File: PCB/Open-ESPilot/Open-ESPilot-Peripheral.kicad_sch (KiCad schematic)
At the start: 47 parts, among them J10 GND, J11 RC in, J12 LED out, J13 Micro_SD_Card, J14 Micro SD Card, J4 UART0, J5 UART1, J6 UART2, J7 I2C, J8 PWM output, J9 Vx, M2 GY91, Q1 NPN, Q2 NPN

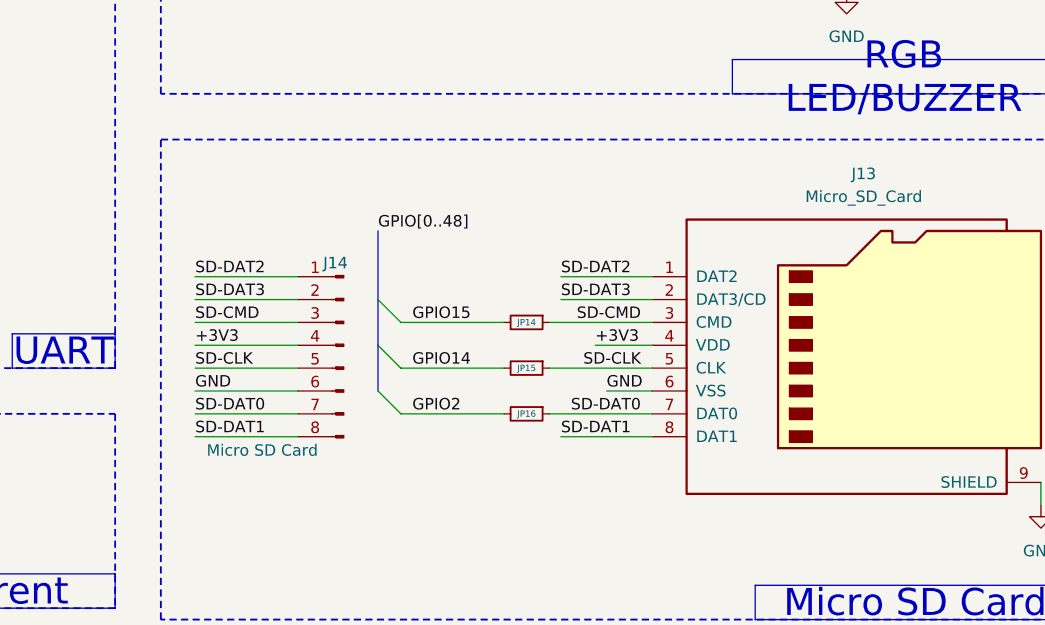
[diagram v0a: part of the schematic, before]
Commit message: Assigned footprints and components for the easy ones (R,C,JP,J)
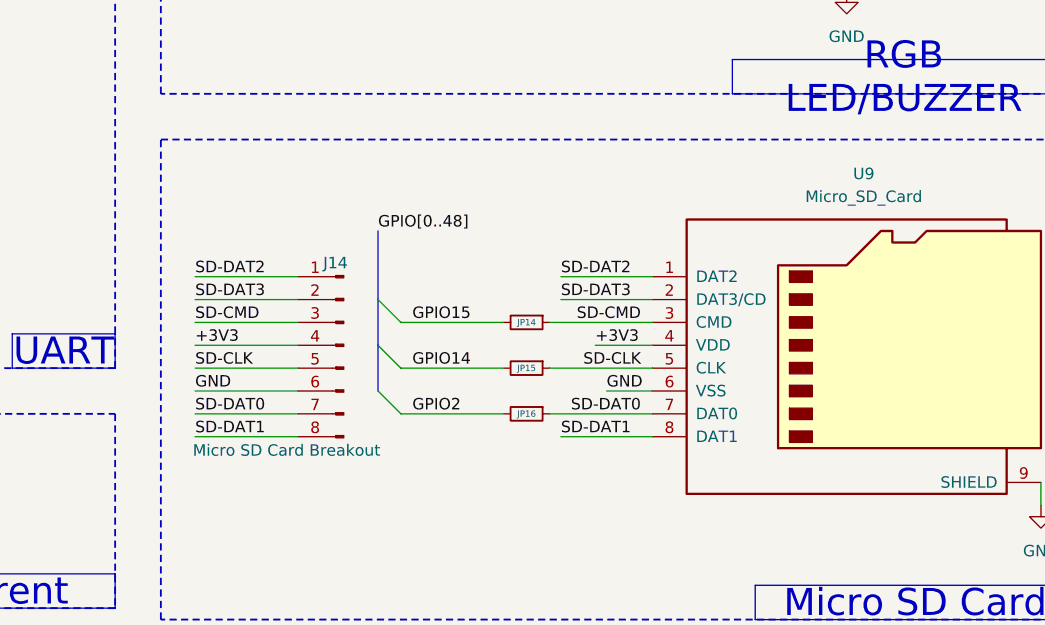
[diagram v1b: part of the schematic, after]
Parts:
- BZ1: footprint Buzzer_Beeper:MagneticBuzzer_StarMicronics_QMB-108 -> (none)
- C8: footprint (none) -> Capacitor_SMD:C_0805_2012Metric_Pad1.18x1.45mm_HandSolder
- J10, J8, J9: footprint (none) -> Connector_PinHeader_2.54mm:PinHeader_1x08_P2.54mm_Vertical
- J11, J12, J4: footprint (none) -> Connector_PinHeader_2.54mm:PinHeader_1x03_P2.54mm_Vertical
- J14: value Micro SD Card -> Micro SD Card Breakout; footprint (none) -> Connector_PinHeader_2.54mm:PinHeader_1x08_P2.54mm_Vertical
- J5, J7: footprint (none) -> Connector_PinHeader_2.54mm:PinHeader_1x04_P2.54mm_Vertical
- J6: footprint (none) -> Connector_PinHeader_2.54mm:PinHeader_1x06_P2.54mm_Vertical
- JP1: footprint (none) -> Jumper:SolderJumper-2_P1.3mm_Bridged2Bar_RoundedPad1.0x1.5mm
- JP2: footprint (none) -> Jumper:SolderJumper-3_P1.3mm_Bridged2Bar12_RoundedPad1.0x1.5mm_NumberLabels
- R10, R11, R5, R6, R7: footprint (none) -> Resistor_SMD:R_0805_2012Metric_Pad1.20x1.40mm_HandSolder
- renumbered J13 to U9
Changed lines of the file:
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@@
 		(dnp no)
 		(fields_autoplaced yes)
-		(property "Reference" "J13"
+		(property "Reference" "U9"
 			(at 255.905 110.49 0)
 			(effects
@@
 			(project ""
 				(path "/2992e60d-a645-4cd7-90ae-fe72311b6bee/e6a81ea1-6816-412d-a6dc-b491c7035238"
-					(reference "J13")
+					(reference "U9")
 					(unit 1)
 				)
@@
 			)
 		)
-		(property "Footprint" ""
+		(property "Footprint" "Connector_PinHeader_2.54mm:PinHeader_1x06_P2.54mm_Vertical"
 			(at 147.32 118.11 0)
 			(effects
@@
 			)
 		)
-		(property "Footprint" ""
+		(property "Footprint" "Connector_PinHeader_2.54mm:PinHeader_1x03_P2.54mm_Vertical"
 			(at 147.32 87.63 0)
 			(effects
@@
 			)
 		)
-		(property "Footprint" "Buzzer_Beeper:MagneticBuzzer_StarMicronics_QMB-108"
+		(property "Footprint" ""
 			(at 258.445 69.85 90)
 			(effects
@@
 			)
 		)
-		(property "Footprint" ""
+		(property "Footprint" "Connector_PinHeader_2.54mm:PinHeader_1x08_P2.54mm_Vertical"
 			(at 91.44 101.6 0)
 			(effects
@@
 			)
 		)
-		(property "Footprint" ""
+		(property "Footprint" "Connector_PinHeader_2.54mm:PinHeader_1x03_P2.54mm_Vertical"
 			(at 83.82 176.53 0)
 			(effects
@@
 			)
 		)
-		(property "Footprint" ""
+		(property "Footprint" "Resistor_SMD:R_0805_2012Metric_Pad1.20x1.40mm_HandSolder"
 			(at 53.34 175.768 90)
 			(effects
@@
 			)
 		)
-		(property "Footprint" ""
+		(property "Footprint" "Resistor_SMD:R_0805_2012Metric_Pad1.20x1.40mm_HandSolder"
 			(at 41.148 160.02 90)
 			(effects
@@
 			)
 		)
-		(property "Footprint" ""
+		(property "Footprint" "Connector_PinHeader_2.54mm:PinHeader_1x03_P2.54mm_Vertical"
 			(at 264.16 39.37 0)
 			(effects
@@
 			)
 		)
-		(property "Footprint" ""
+		(property "Footprint" "Resistor_SMD:R_0805_2012Metric_Pad1.20x1.40mm_HandSolder"
 			(at 103.632 43.18 90)
 			(effects
@@
 			)
 		)
-		(property "Footprint" ""
+		(property "Footprint" "Connector_PinHeader_2.54mm:PinHeader_1x04_P2.54mm_Vertical"
 			(at 147.32 100.33 0)
 			(effects
@@
 			)
 		)
-		(property "Footprint" ""
+		(property "Footprint" "Capacitor_SMD:C_0805_2012Metric_Pad1.18x1.45mm_HandSolder"
 			(at 183.8452 40.64 0)
 			(effects
@@
 			)
 		)
-		(property "Footprint" ""
+		(property "Footprint" "Resistor_SMD:R_0805_2012Metric_Pad1.20x1.40mm_HandSolder"
 			(at 115.062 43.18 90)
 			(effects
@@
 			)
 		)
-		(property "Footprint" ""
+		(property "Footprint" "Jumper:SolderJumper-2_P1.3mm_Bridged2Bar_RoundedPad1.0x1.5mm"
 			(at 69.85 87.63 0)
 			(effects
@@
 			)
 		)
-		(property "Value" "Micro SD Card"
-			(at 182.88 141.224 0)
+		(property "Value" "Micro SD Card Breakout"
+			(at 191.77 141.224 0)
 			(effects
 				(font
 					(size 1.27 1.27)
 				)
-				(justify right)
 			)
 		)
-		(property "Footprint" ""
+		(property "Footprint" "Connector_PinHeader_2.54mm:PinHeader_1x08_P2.54mm_Vertical"
 			(at 198.12 129.54 0)
 			(effects
@@
 			)
 		)
-		(property "Footprint" ""
+		(property "Footprint" "Connector_PinHeader_2.54mm:PinHeader_1x08_P2.54mm_Vertical"
 			(at 77.47 101.6 0)
 			(effects
@@
 			)
 		)
-		(property "Footprint" ""
+		(property "Footprint" "Connector_PinHeader_2.54mm:PinHeader_1x04_P2.54mm_Vertical"
 			(at 162.56 40.64 0)
 			(effects
@@
 			)
 		)
-		(property "Footprint" ""
+		(property "Footprint" "Connector_PinHeader_2.54mm:PinHeader_1x08_P2.54mm_Vertical"
 			(at 62.23 101.6 0)
 			(effects
@@
 			)
 		)
-		(property "Footprint" ""
+		(property "Footprint" "Jumper:SolderJumper-3_P1.3mm_Bridged2Bar12_RoundedPad1.0x1.5mm_NumberLabels"
 			(at 50.8 137.16 0)
 			(effects
@@
 			)
 		)
-		(property "Footprint" ""
+		(property "Footprint" "Resistor_SMD:R_0805_2012Metric_Pad1.20x1.40mm_HandSolder"
 			(at 238.76 84.328 90)
 			(effects

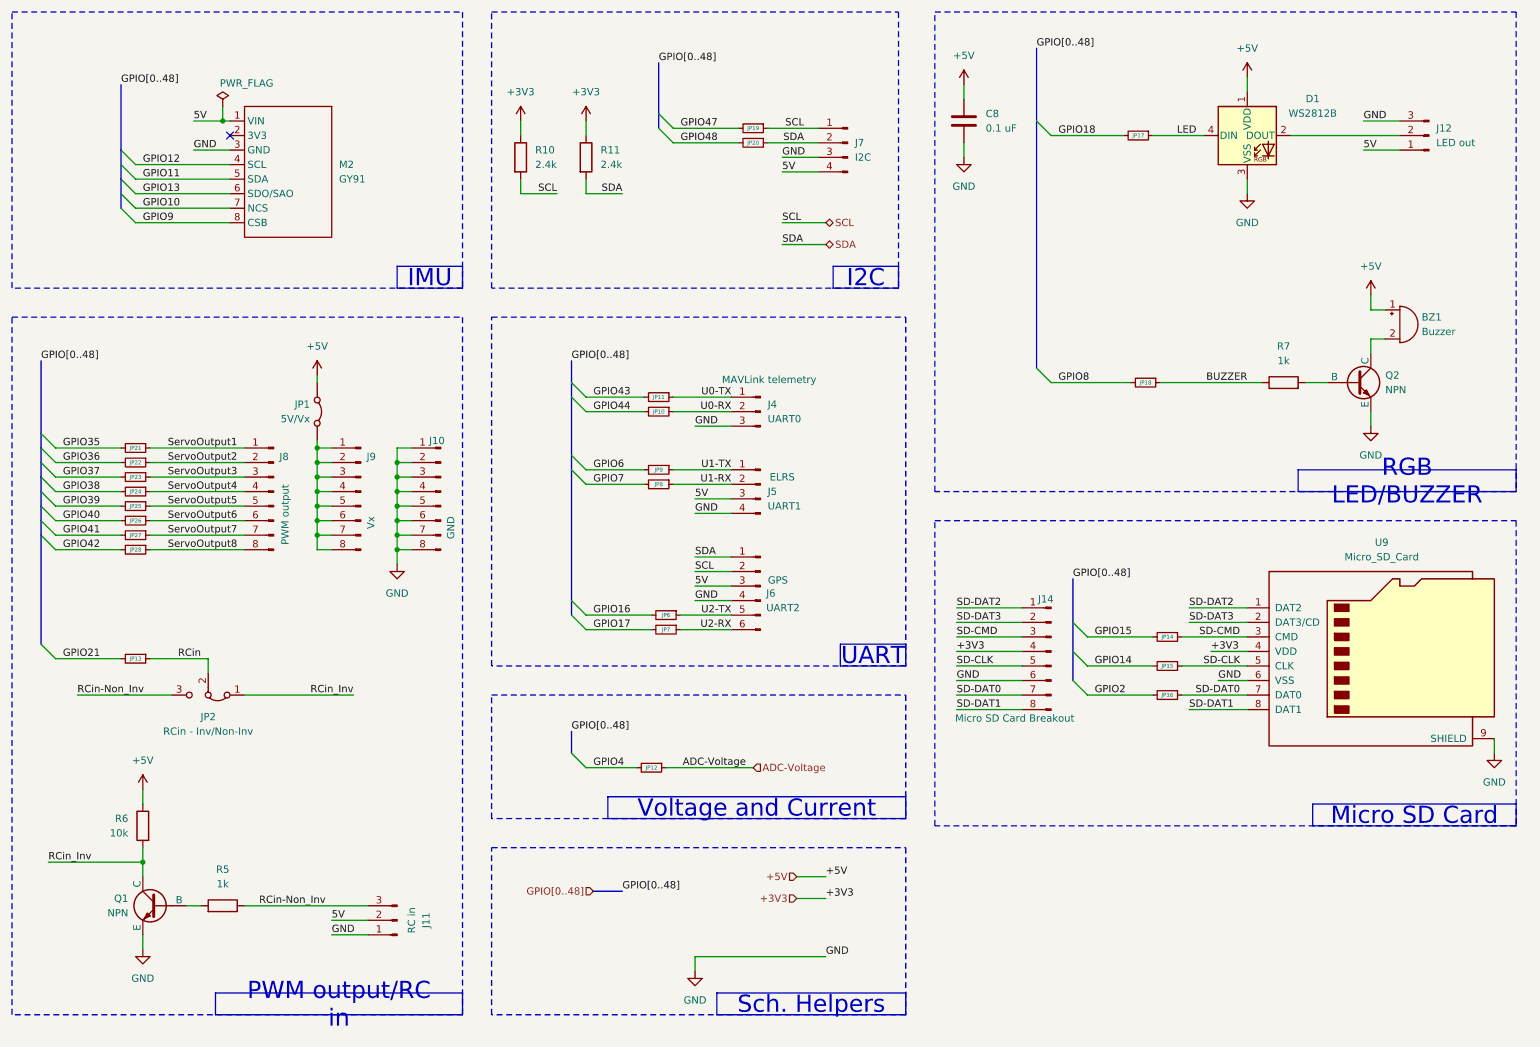
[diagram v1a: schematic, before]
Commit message: Added new footprints for power pads and added decoupling capacitors.
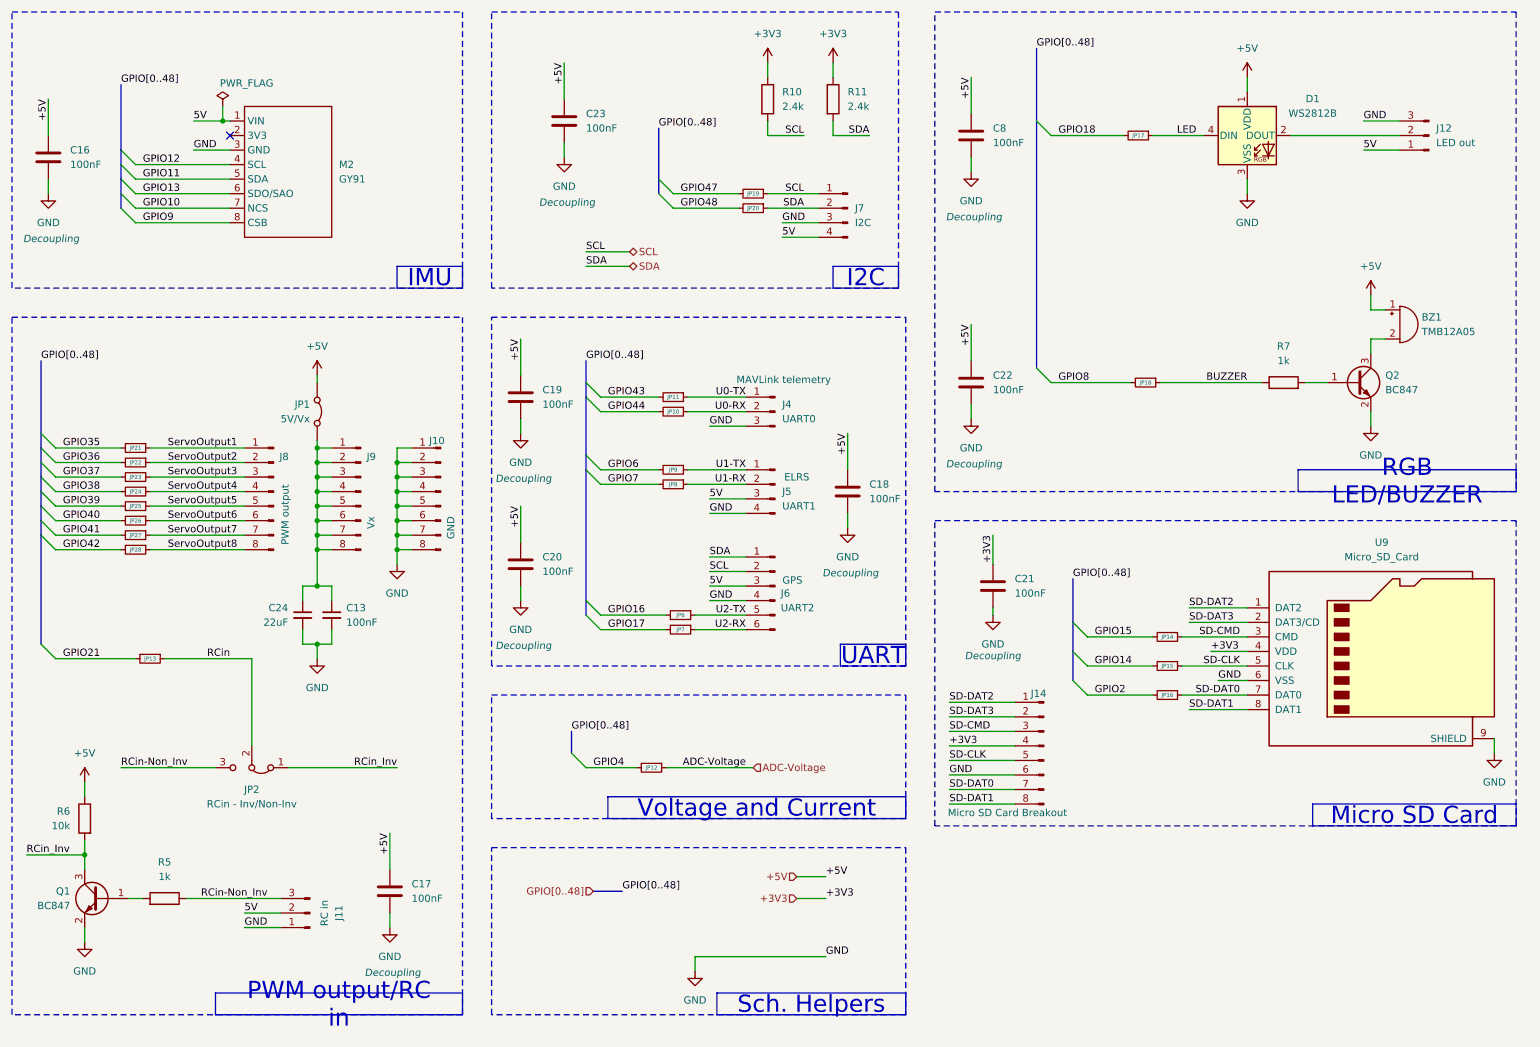
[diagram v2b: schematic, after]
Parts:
- removed Q1, Q2: NPN, symbol Simulation_SPICE:NPN
- added C13: 100nF, Capacitor_SMD:C_0805_2012Metric_Pad1.18x1.45mm_HandSolder, symbol Device:C_Small
- added C16, C17, C18, C19, C20, C21, C22, C23: 100nF, Capacitor_SMD:C_0805_2012Metric_Pad1.18x1.45mm_HandSolder, symbol Device:C
- added C24: 22uF, Capacitor_SMD:C_0805_2012Metric_Pad1.18x1.45mm_HandSolder, symbol Device:C_Small
- added Q1, Q2: BC847, Package_TO_SOT_SMD:SOT-23, symbol Transistor_BJT:BC847
- BZ1: value Buzzer -> TMB12A05; footprint (none) -> Buzzer_Beeper:Buzzer_12x9.5RM7.6; LCSC (none) -> C96093
- C8: value 0.1 uF -> 100nF; Function (none) -> Decoupling
- U9: footprint (none) -> Connector_Card:microSD_HC_Hirose_DM3AT-SF-PEJM5; LCSC (none) -> C114218
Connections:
- net +3V3: now also C21.1
- net +5V: now also C16.1, C17.1, C18.1, C19.1, C20.1, C22.1, C23.1
- net GND: now also C13.2, C16.2, C17.2, C18.2, C19.2, C20.2, C21.2, C22.2, C23.2, C24.2, Q1.2 (E), Q2.2 (E)
- net RCin_Inv: now also Q1.3 (C)
- net at BZ1.2 (-): now also Q2.3 (C)
- net at R5.2: now also Q1.1 (B)
- net at J9.1 (Pin_1), J9.2 (Pin_2), J9.3 (Pin_3)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: now also C13.1, C24.1
- net at R7.2: now also Q2.1 (B)
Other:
- moved on the sheet: J11, J14, J4, J5, J6, J7, JP10, JP11, JP13, JP19, JP2, JP20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

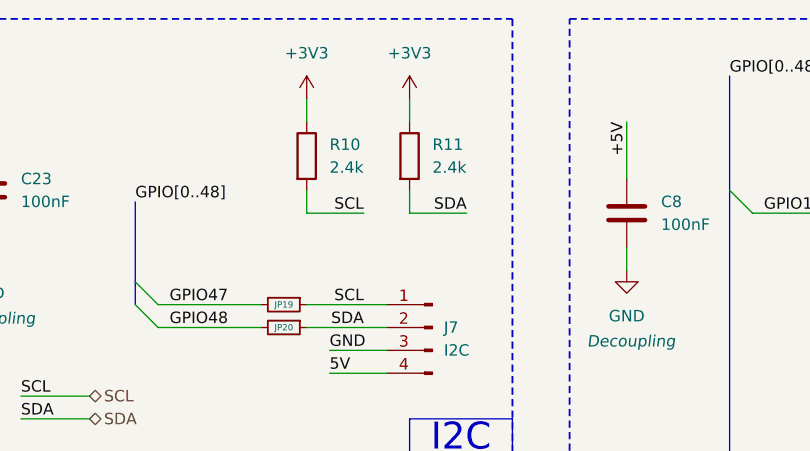
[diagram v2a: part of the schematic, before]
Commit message: Completed the INA219 current sensor schematic. Changed the I2C pullups for a value thats common on board.
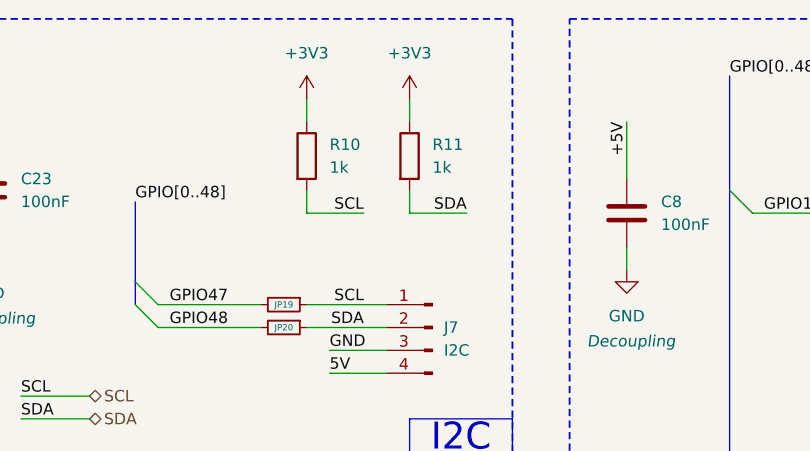
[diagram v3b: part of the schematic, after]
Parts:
- R10, R11: value 2.4k -> 1k
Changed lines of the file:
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@@
 			)
 		)
-		(property "Value" "2.4k"
+		(property "Value" "1k"
 			(at 151.13 34.2899 0)
 			(effects
@@
 			)
 		)
-		(property "Value" "2.4k"
+		(property "Value" "1k"
 			(at 162.56 34.2899 0)
 			(effects

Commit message: Reanotated Schematic.
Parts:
- renumbered C16 to C15, C24 to C16, C13 to C17, C17 to C18, C23 to C21, C18 to C22, C8 to C23, C22 to C24, C21 to C25, D1 to D5, J5 to J10, J6 to J11, J7 to J12, J14 to J13, J12 to J14, J8 to J5, J11 to J6, J9 to J7, J10 to J8, J4 to J9, JP27 to JP10, JP28 to JP11, JP13 to JP12, JP2 to JP13, JP1 to JP14, JP12 to JP15, JP11 to JP16, JP10 to JP17, JP9 to JP18, JP8 to JP19, JP6 to JP20, JP7 to JP21, JP19 to JP22, JP20 to JP23, JP17 to JP24, JP18 to JP25, JP14 to JP26, JP15 to JP27, JP16 to JP28, JP21 to JP4, JP22 to JP5, JP23 to JP6, JP24 to JP7, JP25 to JP8, JP26 to JP9, Q1 to Q2, Q2 to Q3, R6 to R13, R5 to R14, R10 to R15, R11 to R16, R7 to R17, U9 to U5

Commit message: PCB init.
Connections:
- net +5V: now also M2.1 (VIN)
- net 5V: no longer M2.1 (VIN)
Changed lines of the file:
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@@
 		)
 	)
-	(label "5V"
+	(label "+5V"
 		(at 48.26 36.83 0)
 		(effects
